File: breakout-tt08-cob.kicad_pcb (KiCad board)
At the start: 2 copper layers, 50 x 52 mm, 157 parts, among them CON1 NPTC202KFMS-RC, CON2 NPTC202KFMS-RC, J1 Conn_01x04, J2 Conn_02x06_Odd_Even, J3 Conn_02x06_Odd_Even, U1 Openframe_QFN_TT06_REV2, U2 24LC02

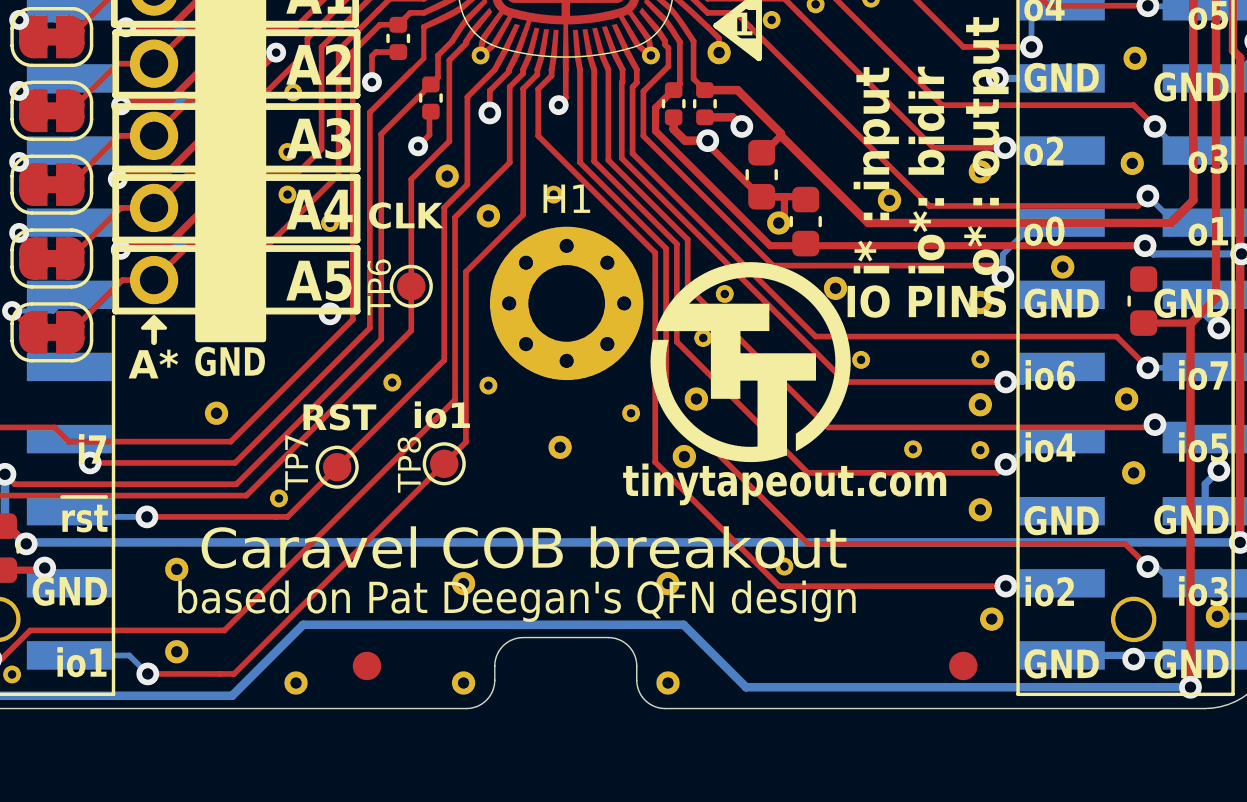
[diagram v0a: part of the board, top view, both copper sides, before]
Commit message: minor silkscreen fixes
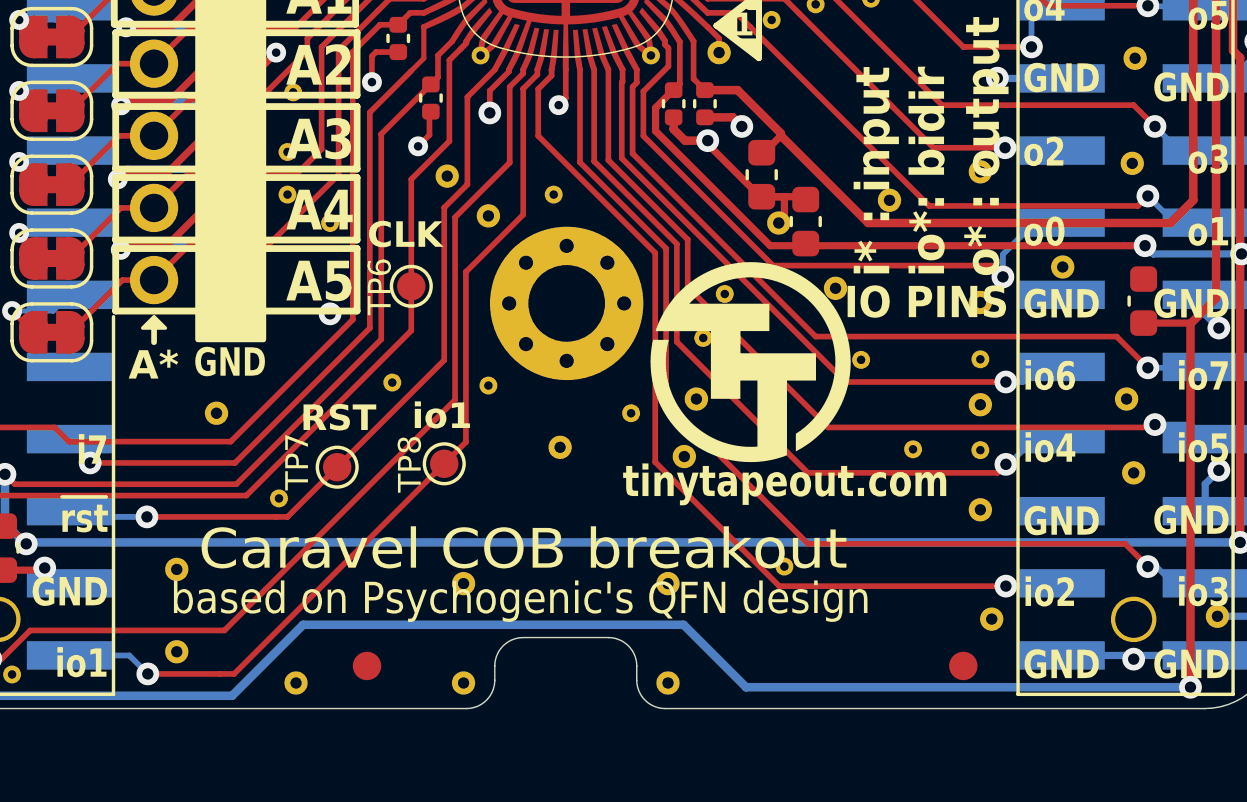
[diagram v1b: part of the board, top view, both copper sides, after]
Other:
- board text added: "based on Psychogenic's QFN design"
- board text removed: "based on Pat Deegan's QFN design"
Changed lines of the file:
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@@
 			(at 0 -3.65 0)
 			(layer "F.SilkS")
+			(hide yes)
 			(effects
 				(font
@@
 	)
 	(gr_text "CLK"
-		(at 63.51 53.2 0)
+		(at 63.51 53.85 0)
 		(layer "F.SilkS" knockout)
 		(effects
@@
 		)
 	)
-	(gr_text "based on Pat Deegan's QFN design"
-		(at 56.73 66.77 0)
+	(gr_text "based on Psychogenic's QFN design"
+		(at 56.575 66.77 0)
 		(layer "F.SilkS")
 		(effects
@@
 			(keep_text_aligned yes)
 		)
-		(gr_text "1968,5039 mils"
+		(gr_text "50,0000 mm"
 			(at 70.5 15.35 0)
 			(layer "User.1")
@@
 			(keep_text_aligned yes)
 		)
-		(gr_text "1574,8031 mils"
+		(gr_text "40,0000 mm"
 			(at 70.5 71.95 0)
 			(layer "User.1")
@@
 			(keep_text_aligned yes)
 		)
-		(gr_text "2047,2441 mils"
+		(gr_text "52,0000 mm"
 			(at 41.85 44 90)
 			(layer "User.1")
